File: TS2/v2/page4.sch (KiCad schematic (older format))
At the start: 5 parts, among them U11 HM6264, U12 2764, U13 HM6264, U14 2764, U5 74LS04

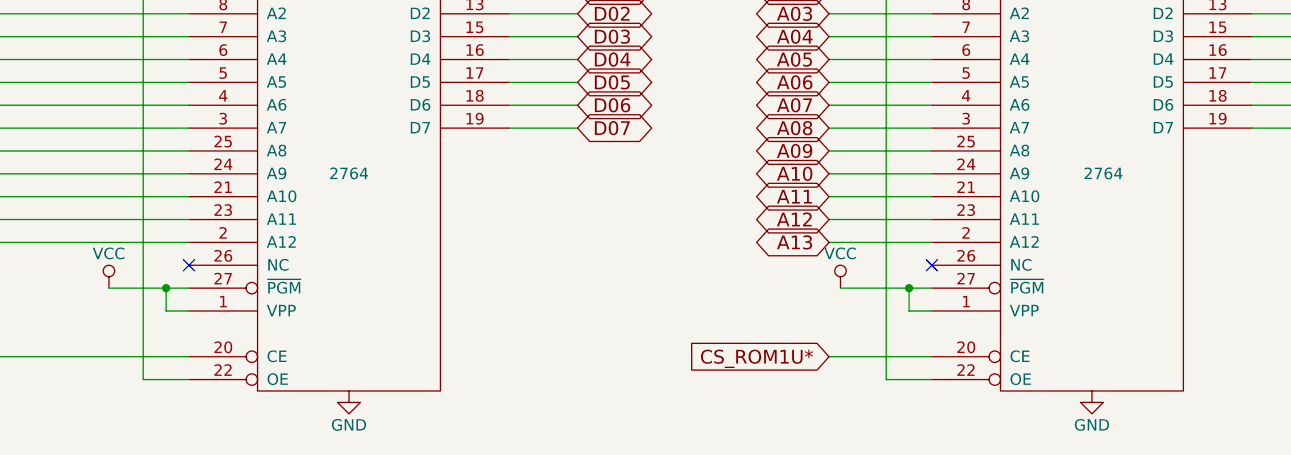
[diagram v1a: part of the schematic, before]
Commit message: Use 28C64 EEPROM instead of 27C64 EPROM.
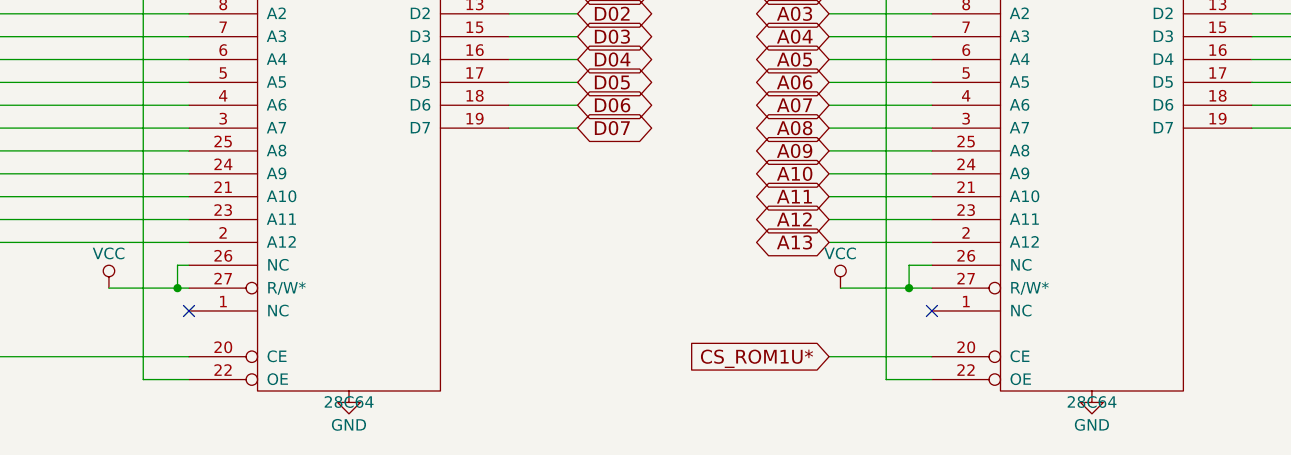
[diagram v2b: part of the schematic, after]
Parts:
- removed U12, U14: 2764, symbol 2764
- added U12, U14: 28C64, symbol 28C64
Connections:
- net A01: now also U12.10 (A0), U14.10 (A0)
- net A02: now also U12.9 (A1), U14.9 (A1)
- net A03: now also U12.8 (A2), U14.8 (A2)
- net A04: now also U12.7 (A3), U14.7 (A3)
- net A05: now also U12.6 (A4), U14.6 (A4)
- net A06: now also U12.5 (A5), U14.5 (A5)
- net A07: now also U12.4 (A6), U14.4 (A6)
- net A08: now also U12.3 (A7), U14.3 (A7)
- net A09: now also U12.25 (A8), U14.25 (A8)
- net A10: now also U12.24 (A9), U14.24 (A9)
- net A11: now also U12.21 (A10), U14.21 (A10)
- net A12: now also U12.23 (A11), U14.23 (A11)
- net A13: now also U12.2 (A12), U14.2 (A12)
- net CS_ROM1L*: now also U12.20 (CE)
- net CS_ROM1U*: now also U14.20 (CE)
- net D00: now also U12.11 (D0)
- net D01: now also U12.12 (D1)
- net D02: now also U12.13 (D2)
- net D03: now also U12.15 (D3)
- net D04: now also U12.16 (D4)
- net D05: now also U12.17 (D5)
- net D06: now also U12.18 (D6)
- net D07: now also U12.19 (D7)
- net D08: now also U14.11 (D0)
- net D09: now also U14.12 (D1)
- net D10: now also U14.13 (D2)
- net D11: now also U14.15 (D3)
- net D12: now also U14.16 (D4)
- net D13: now also U14.17 (D5)
- net D14: now also U14.18 (D6)
- net D15: now also U14.19 (D7)
- net GND: now also U12.14 (GND), U14.14 (GND)
- net R*/W: now also U12.22 (OE), U14.22 (OE)
- net VCC: now also U12.26 (NC), U12.27 (R/W*), U12.28 (VCC), U14.26 (NC), U14.27 (R/W*), U14.28 (VCC)
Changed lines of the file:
@@
 $EndDescr
-$Comp
-L 2764 U12
-U 1 1 57C37A1F
-P 4350 5100
-F 0 "U12" H 4100 6100 50  0000 C CNN
-F 1 "2764" H 4350 5100 50  0000 C CNN
-F 2 "" H 4350 5100 50  0000 C CNN
-F 3 "" H 4350 5100 50  0000 C CNN
-	1    4350 5100
-	1    0    0    -1
-$EndComp
-$Comp
-L 2764 U14
-U 1 1 57C37AB5
-P 7600 5100
-F 0 "U14" H 7350 6100 50  0000 C CNN
-F 1 "2764" H 7650 5100 50  0000 C CNN
-F 2 "" H 7600 5100 50  0000 C CNN
-F 3 "" H 7600 5100 50  0000 C CNN
-	1    7600 5100
-	1    0    0    -1
-$EndComp
 $Comp
 L HM6264 U11
@@
 Wire Wire Line
 	3300 5600 3650 5600
-Wire Wire Line
-	3650 5700 3550 5700
-Wire Wire Line
-	3550 5700 3550 5600
 $Comp
 L VCC #PWR037
@@
 Wire Wire Line
 	2300 5900 3650 5900
-NoConn ~ 3650 5500
 Wire Wire Line
 	3650 5400 2300 5400
@@
 Wire Wire Line
 	2300 4400 3650 4400
-Connection ~ 3550 5600
 Text GLabel 5350 4200 2    60   BiDi ~ 0
 D00
@@
 	1    0    0    -1
 $EndComp
-NoConn ~ 6900 5500
 Text GLabel 6450 4300 0    60   BiDi ~ 0
 A02
@@
 Wire Wire Line
 	6500 5600 6900 5600
-Wire Wire Line
-	6800 5600 6800 5700
-Wire Wire Line
-	6800 5700 6900 5700
 Connection ~ 6800 5600
 $Comp
@@
 	2400 3750 3450 3750
 Connection ~ 3450 3950
+$Comp
+L 28C64 U12
+U 1 1 57D4E8EE
+P 4350 5100
+F 0 "U12" H 4100 6100 50  0000 C CNN
+F 1 "28C64" H 4350 4100 50  0000 C CNN
+F 2 "" H 4350 5100 50  0000 C CNN
+F 3 "" H 4350 5100 50  0000 C CNN
+	1    4350 5100
+	1    0    0    -1
+$EndComp
+NoConn ~ 3650 5700
+Wire Wire Line
+	3650 5500 3600 5500
+Wire Wire Line
+	3600 5500 3600 5600
+Connection ~ 3600 5600
+$Comp
+L 28C64 U14
+U 1 1 57D4F506
+P 7600 5100
+F 0 "U14" H 7350 6100 50  0000 C CNN
+F 1 "28C64" H 7600 4100 50  0000 C CNN
+F 2 "" H 7600 5100 50  0000 C CNN
+F 3 "" H 7600 5100 50  0000 C CNN
+	1    7600 5100
+	1    0    0    -1
+$EndComp
+Wire Wire Line
+	6900 5500 6800 5500
+NoConn ~ 6900 5700
+Wire Wire Line
+	6800 5500 6800 5600
 $EndSCHEMATC

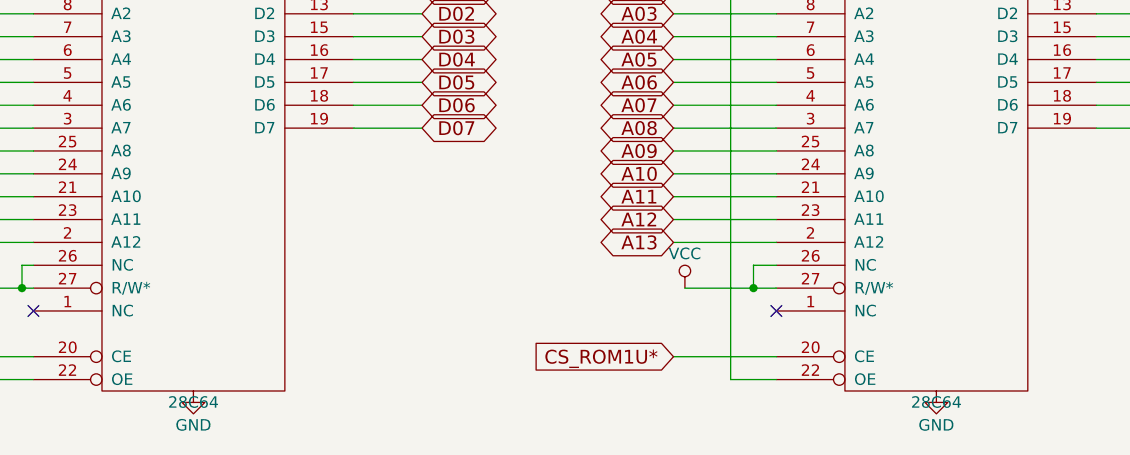
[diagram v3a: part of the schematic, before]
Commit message: Remove two duplicated pullup resistors. Route some signals better.
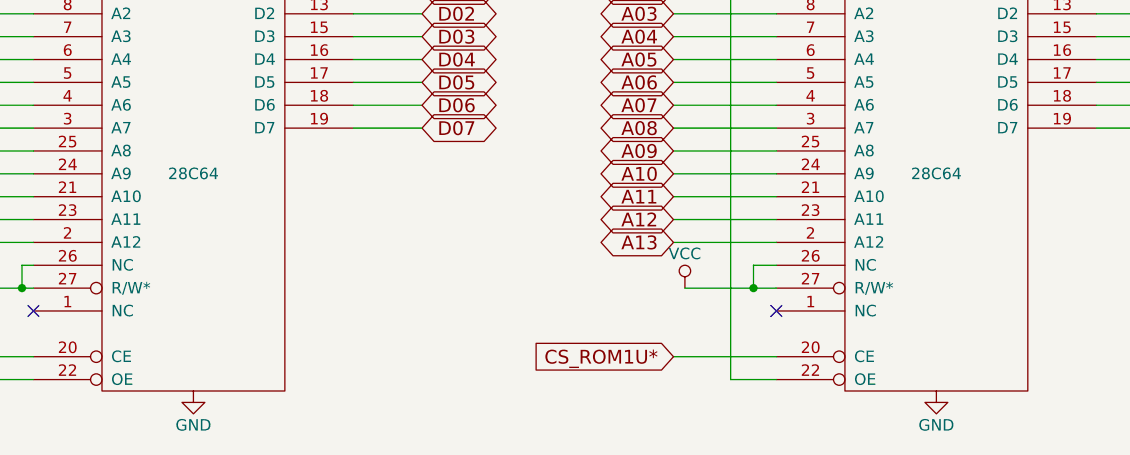
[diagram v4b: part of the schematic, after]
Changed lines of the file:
@@
 Sheet 5 8
 Title "TS2 68000 Single Board Computer"
-Date "2016-09-03"
+Date "2016-11-27"
 Rev "2.0"
 Comp "Jeff Tranter"
@@
 	5050 1650 5350 1650
 $Comp
-L GND #PWR031
+L GND #PWR030
 U 1 1 57CAE147
 P 5050 3250
-F 0 "#PWR031" H 5050 3000 50  0001 C CNN
+F 0 "#PWR030" H 5050 3000 50  0001 C CNN
 F 1 "GND" H 5050 3100 50  0000 C CNN
 F 2 "" H 5050 3250 50  0000 C CNN
@@
 $EndComp
 $Comp
-L VCC #PWR032
+L VCC #PWR031
 U 1 1 57CAE148
 P 5050 3150
-F 0 "#PWR032" H 5050 3000 50  0001 C CNN
+F 0 "#PWR031" H 5050 3000 50  0001 C CNN
 F 1 "VCC" H 5050 3300 50  0000 C CNN
 F 2 "" H 5050 3150 50  0000 C CNN
@@
 $EndComp
 $Comp
-L VCC #PWR033
+L VCC #PWR032
 U 1 1 57CAE149
 P 8300 3150
-F 0 "#PWR033" H 8300 3000 50  0001 C CNN
+F 0 "#PWR032" H 8300 3000 50  0001 C CNN
 F 1 "VCC" H 8300 3300 50  0000 C CNN
 F 2 "" H 8300 3150 50  0000 C CNN
@@
 $EndComp
 $Comp
-L GND #PWR034
+L GND #PWR033
 U 1 1 57CAE14A
 P 8300 3250
-F 0 "#PWR034" H 8300 3000 50  0001 C CNN
+F 0 "#PWR033" H 8300 3000 50  0001 C CNN
 F 1 "GND" H 8300 3100 50  0000 C CNN
 F 2 "" H 8300 3250 50  0000 C CNN
@@
 A01
 $Comp
-L VCC #PWR035
+L VCC #PWR034
 U 1 1 57CAE14B
 P 4350 1500
-F 0 "#PWR035" H 4350 1350 50  0001 C CNN
+F 0 "#PWR034" H 4350 1350 50  0001 C CNN
 F 1 "VCC" H 4350 1650 50  0000 C CNN
 F 2 "" H 4350 1500 50  0000 C CNN
@@
 $EndComp
 $Comp
-L GND #PWR036
+L GND #PWR035
 U 1 1 57CAE14C
 P 4350 3400
-F 0 "#PWR036" H 4350 3150 50  0001 C CNN
+F 0 "#PWR035" H 4350 3150 50  0001 C CNN
 F 1 "GND" H 4350 3250 50  0000 C CNN
 F 2 "" H 4350 3400 50  0000 C CNN
@@
 CS_ROM1L*
 $Comp
-L GND #PWR037
+L GND #PWR036
 U 1 1 57CAE14D
 P 4350 6050
-F 0 "#PWR037" H 4350 5800 50  0001 C CNN
+F 0 "#PWR036" H 4350 5800 50  0001 C CNN
 F 1 "GND" H 4350 5900 50  0000 C CNN
 F 2 "" H 4350 6050 50  0000 C CNN
@@
 $EndComp
 $Comp
-L VCC #PWR038
+L VCC #PWR037
 U 1 1 57C52031
 P 4350 4150
-F 0 "#PWR038" H 4350 4000 50  0001 C CNN
+F 0 "#PWR037" H 4350 4000 50  0001 C CNN
 F 1 "VCC" H 4350 4300 50  0000 C CNN
 F 2 "" H 4350 4150 50  0000 C CNN
@@
 	3300 5600 3650 5600
 $Comp
-L VCC #PWR039
+L VCC #PWR038
 U 1 1 57C5238F
 P 3300 5600
-F 0 "#PWR039" H 3300 5450 50  0001 C CNN
+F 0 "#PWR038" H 3300 5450 50  0001 C CNN
 F 1 "VCC" H 3300 5750 50  0000 C CNN
 F 2 "" H 3300 5600 50  0000 C CNN
@@
 Connection ~ 3650 3650
 $Comp
-L VCC #PWR040
+L VCC #PWR039
 U 1 1 57C5501D
 P 7600 1500
-F 0 "#PWR040" H 7600 1350 50  0001 C CNN
+F 0 "#PWR039" H 7600 1350 50  0001 C CNN
 F 1 "VCC" H 7600 1650 50  0000 C CNN
 F 2 "" H 7600 1500 50  0000 C CNN
@@
 $EndComp
 $Comp
-L GND #PWR041
+L GND #PWR040
 U 1 1 57C5503B
 P 7600 3400
-F 0 "#PWR041" H 7600 3150 50  0001 C CNN
+F 0 "#PWR040" H 7600 3150 50  0001 C CNN
 F 1 "GND" H 7600 3250 50  0000 C CNN
 F 2 "" H 7600 3400 50  0000 C CNN
@@
 	6450 4200 6900 4200
 $Comp
-L VCC #PWR042
+L VCC #PWR041
 U 1 1 57C5736B
 P 7600 4150
-F 0 "#PWR042" H 7600 4000 50  0001 C CNN
+F 0 "#PWR041" H 7600 4000 50  0001 C CNN
 F 1 "VCC" H 7600 4300 50  0000 C CNN
 F 2 "" H 7600 4150 50  0000 C CNN
@@
 $EndComp
 $Comp
-L GND #PWR043
+L GND #PWR042
 U 1 1 57C573B1
 P 7600 6050
-F 0 "#PWR043" H 7600 5800 50  0001 C CNN
+F 0 "#PWR042" H 7600 5800 50  0001 C CNN
 F 1 "GND" H 7600 5900 50  0000 C CNN
 F 2 "" H 7600 6050 50  0000 C CNN
@@
 Connection ~ 6800 5600
 $Comp
-L VCC #PWR044
+L VCC #PWR043
 U 1 1 57CAE154
 P 6500 5600
-F 0 "#PWR044" H 6500 5450 50  0001 C CNN
+F 0 "#PWR043" H 6500 5450 50  0001 C CNN
 F 1 "VCC" H 6500 5750 50  0000 C CNN
 F 2 "" H 6500 5600 50  0000 C CNN
@@
 P 4350 5100
 F 0 "U12" H 4100 6100 50  0000 C CNN
-F 1 "28C64" H 4350 4100 50  0000 C CNN
+F 1 "28C64" H 4350 5100 50  0000 C CNN
 F 2 "" H 4350 5100 50  0000 C CNN
 F 3 "" H 4350 5100 50  0000 C CNN
@@
 P 7600 5100
 F 0 "U14" H 7350 6100 50  0000 C CNN
-F 1 "28C64" H 7600 4100 50  0000 C CNN
+F 1 "28C64" H 7600 5100 50  0000 C CNN
 F 2 "" H 7600 5100 50  0000 C CNN
 F 3 "" H 7600 5100 50  0000 C CNN

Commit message: Route a signal better.
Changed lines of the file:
@@
 	2550 3650 2550 3950
 Wire Wire Line
-	2300 3650 6900 3650
+	2300 3650 2550 3650
+Wire Wire Line
+	2550 3650 3650 3650
+Wire Wire Line
+	3650 3650 6900 3650
 Wire Wire Line
 	3650 3650 3650 3300
@@
 CS_RAM1L*
 Wire Wire Line
-	3450 3750 3450 6000
+	3450 3750 3450 3950
+Wire Wire Line
+	3450 3950 3450 6000
 Wire Wire Line
 	2300 1550 3650 1550
@@
 $EndComp
 Wire Wire Line
-	3300 5600 3650 5600
+	3300 5600 3550 5600
+Wire Wire Line
+	3550 5600 3650 5600
 $Comp
 L VCC #PWR038
@@
 A13
 Wire Wire Line
-	6500 5600 6900 5600
+	6500 5600 6800 5600
+Wire Wire Line
+	6800 5600 6900 5600
 Connection ~ 6800 5600
 $Comp
@@
 NoConn ~ 3650 5700
 Wire Wire Line
-	3650 5500 3600 5500
-Wire Wire Line
-	3600 5500 3600 5600
-Connection ~ 3600 5600
+	3650 5500 3550 5500
+Wire Wire Line
+	3550 5500 3550 5600
+Connection ~ 3550 5600
 $Comp
 L 28C64 U14

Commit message: Move some labels to make them more readable.
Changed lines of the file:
@@
 	2550 3650 2550 3950
 Wire Wire Line
-	2300 3650 2550 3650
-Wire Wire Line
-	2550 3650 3650 3650
-Wire Wire Line
-	3650 3650 6900 3650
+	2300 3650 6900 3650
 Wire Wire Line
 	3650 3650 3650 3300
@@
 CS_RAM1L*
 Wire Wire Line
-	3450 3750 3450 3950
-Wire Wire Line
-	3450 3950 3450 6000
+	3450 3750 3450 6000
 Wire Wire Line
 	2300 1550 3650 1550
@@
 $EndComp
 Wire Wire Line
-	3300 5600 3550 5600
-Wire Wire Line
-	3550 5600 3650 5600
+	3300 5600 3650 5600
 $Comp
 L VCC #PWR038
@@
 A13
 Wire Wire Line
-	6500 5600 6800 5600
-Wire Wire Line
-	6800 5600 6900 5600
+	6500 5600 6900 5600
 Connection ~ 6800 5600
 $Comp

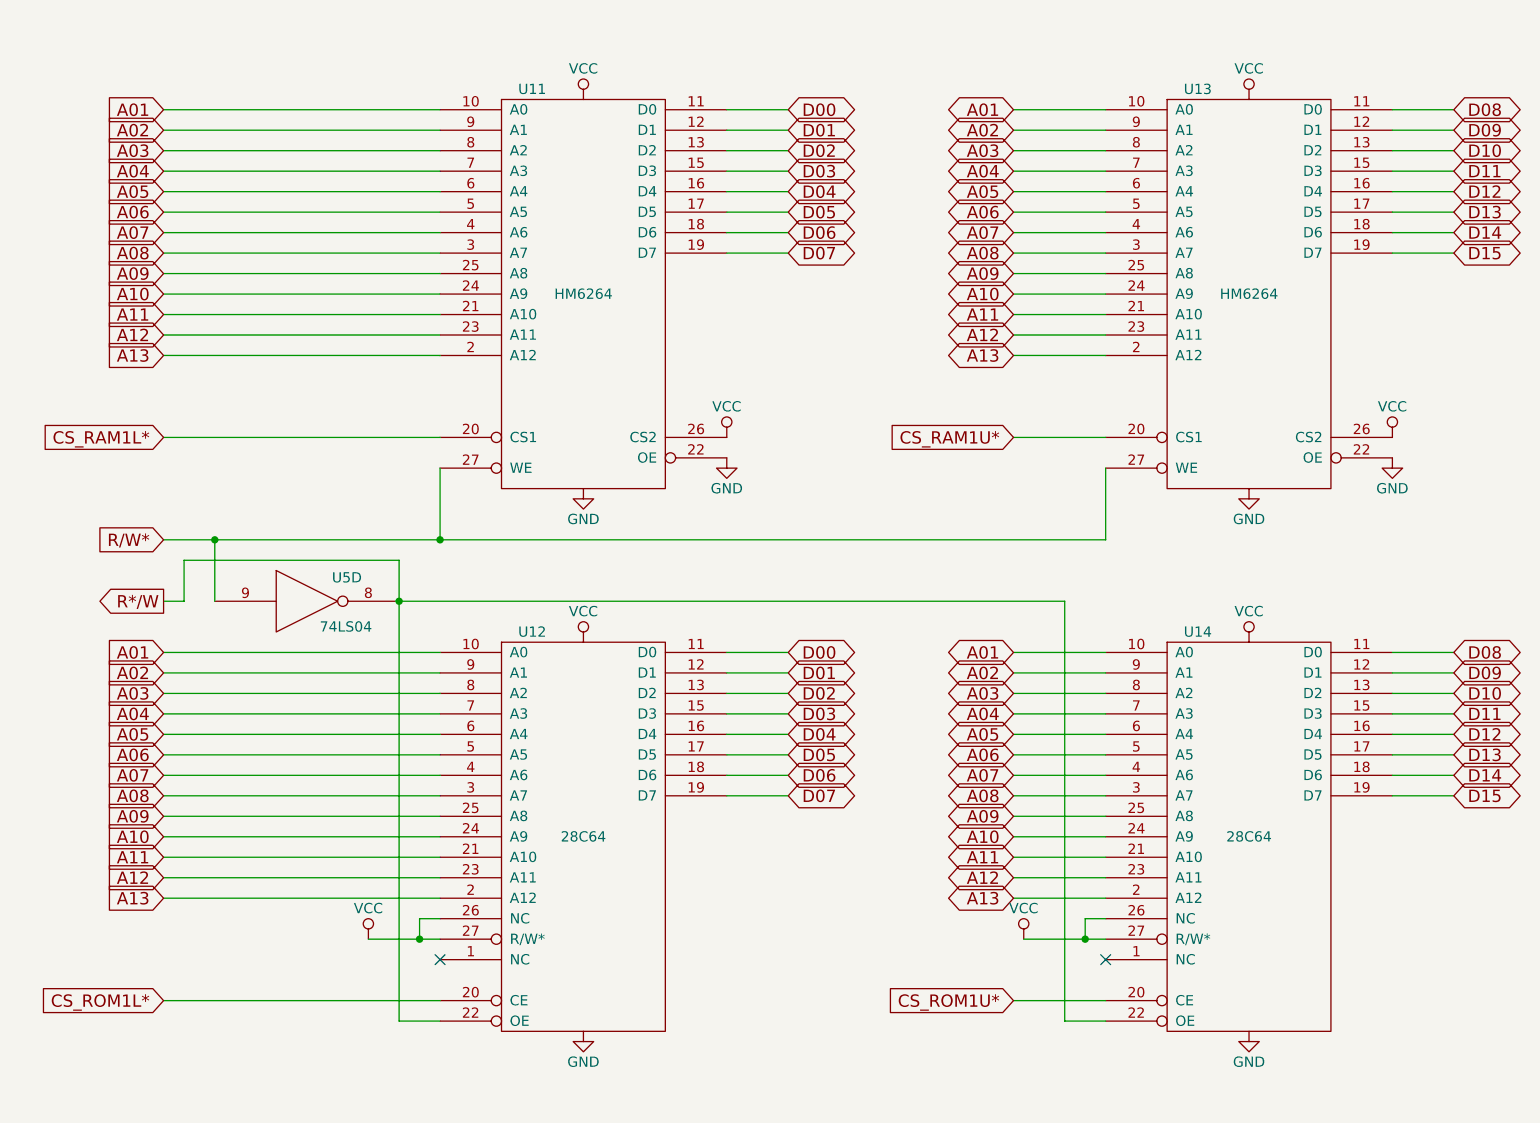
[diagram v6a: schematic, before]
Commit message: Label RAM and ROM chips with address ranges.
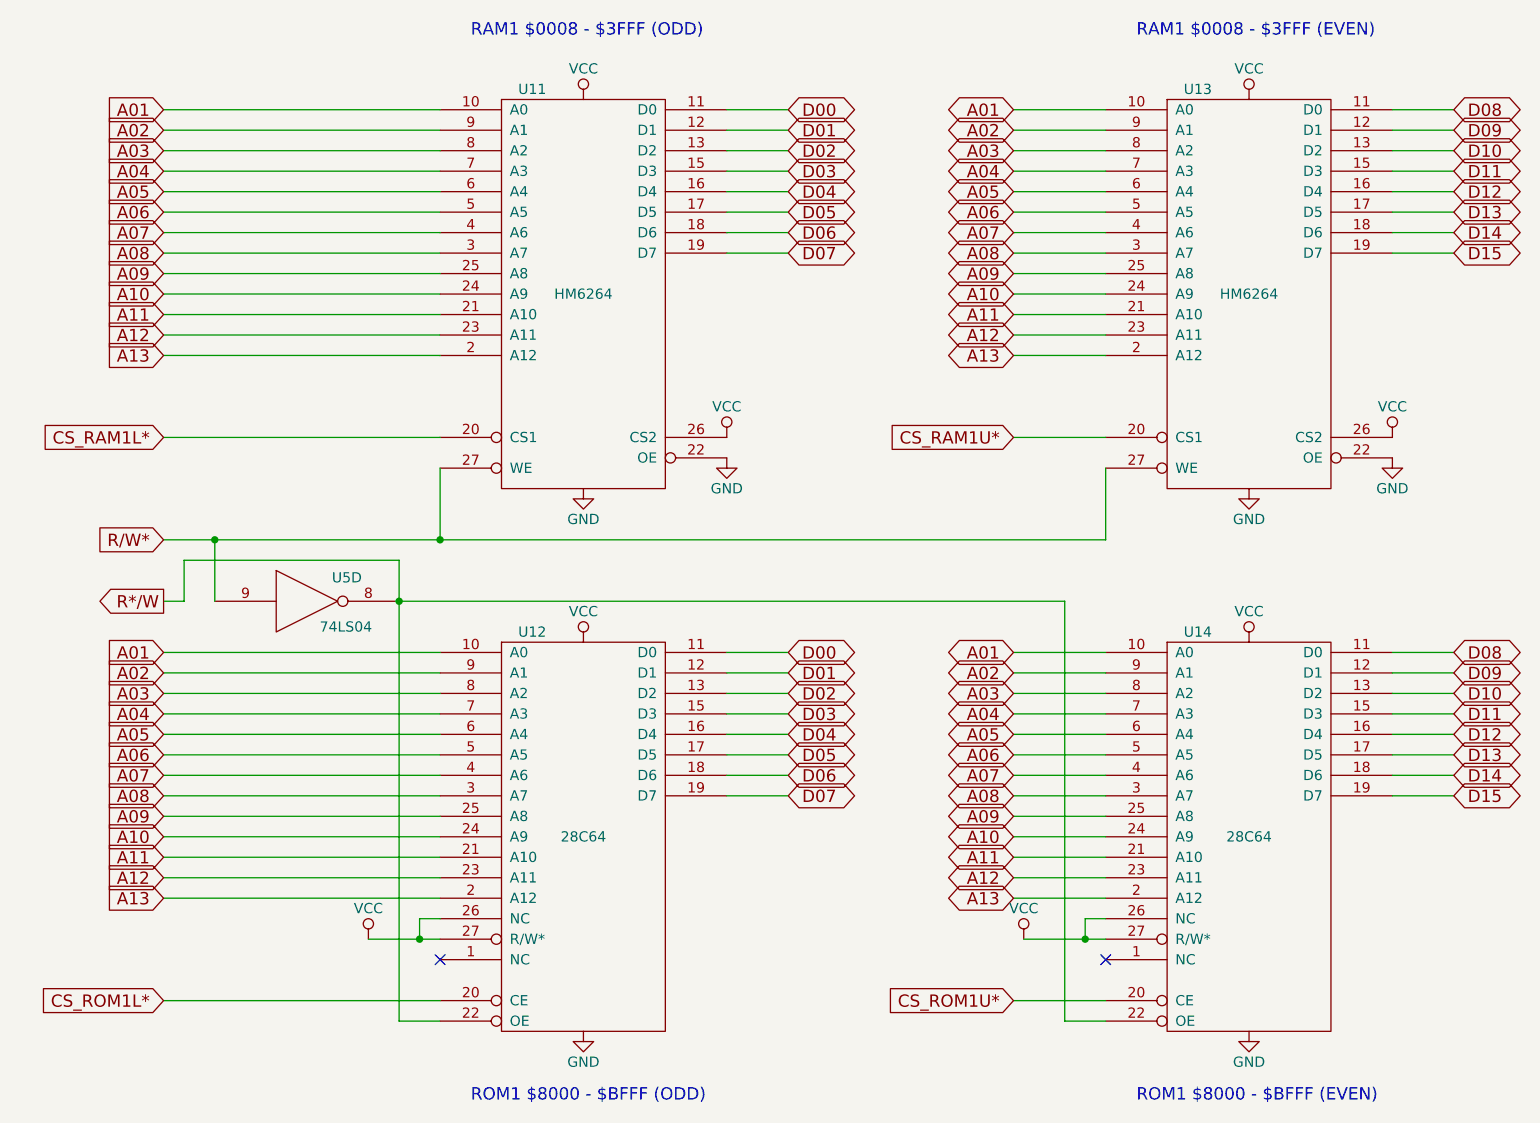
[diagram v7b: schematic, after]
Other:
- note added: "RAM1 $0008 - $3FFF (EVEN)"
- note added: "RAM1 $0008 - $3FFF (ODD)"
- note added: "ROM1 $8000 - $BFFF (EVEN)"
- note added: "ROM1 $8000 - $BFFF (ODD)"
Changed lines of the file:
@@
 Wire Wire Line
 	6800 5500 6800 5600
+Text Notes 3800 1200 0    60   ~ 0
+RAM1 $0008 - $3FFF (ODD)
+Text Notes 7050 1200 0    60   ~ 0
+RAM1 $0008 - $3FFF (EVEN)
+Text Notes 3800 6400 0    60   ~ 0
+ROM1 $8000 - $BFFF (ODD)
+Text Notes 7050 6400 0    60   ~ 0
+ROM1 $8000 - $BFFF (EVEN)
 $EndSCHEMATC
